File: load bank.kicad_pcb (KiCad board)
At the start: 2 copper layers, 95.4 x 80.6 mm, 28 parts, among them J1 25SH-B-02-TS, J10 25SH-B-02-TS, J11 EURO_BLOCK,_3_POSITION, J12 EURO_BLOCK,_3_POSITION, J2 LHD-03-TS, J3 EBBA-03-C-SS-BU, J4 25SH-B-02-TS, J5 Conn_01x02_Male, J6 Conn_01x02_Male, J7 696101000002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

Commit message: updated pcb with fan2 connector
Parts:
- added J13: 25SH-B-02-TS, Connector_JST:JST_EH_B2B-EH-A_1x02_P2.50mm_Vertical, F.Cu at (142.2, 87.9)
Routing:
- net +5V: track 30.8 -> 42.7 mm
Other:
- board text removed: "120V 7A"

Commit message: updated pcb layout with zener and resistor
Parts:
- added D5: 1N5230B, 1N5231B_R0:DIOAD928W47L399D179, F.Cu at (164.6, 92.2)
- added R6: 500R, Resistor_THT:R_Axial_DIN0207_L6.3mm_D2.5mm_P7.62mm_Horizontal, F.Cu at (161.3, 88.4)
- moved J5 7.52 mm to (162.1, 83.3)
- moved J11 2.76 mm to (158.3, 68.1)
- moved R5 0.25 mm to (167.9, 96.5)
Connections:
- D2 pad 2: +5V -> Net-(D2-A)
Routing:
- net Net-(D2-A): track 0.00 -> 7.56 mm
- net Net-(J5-Pin_1): track 8.75 -> 14.5 mm
- net Net-(D3-A): track 76.8 -> 79.2 mm
- net GNDA: track 108.8 -> 110.1 mm
- net /res_1: track 20.5 -> 19.5 mm
- net +5V: track 42.7 -> 41.9 mm

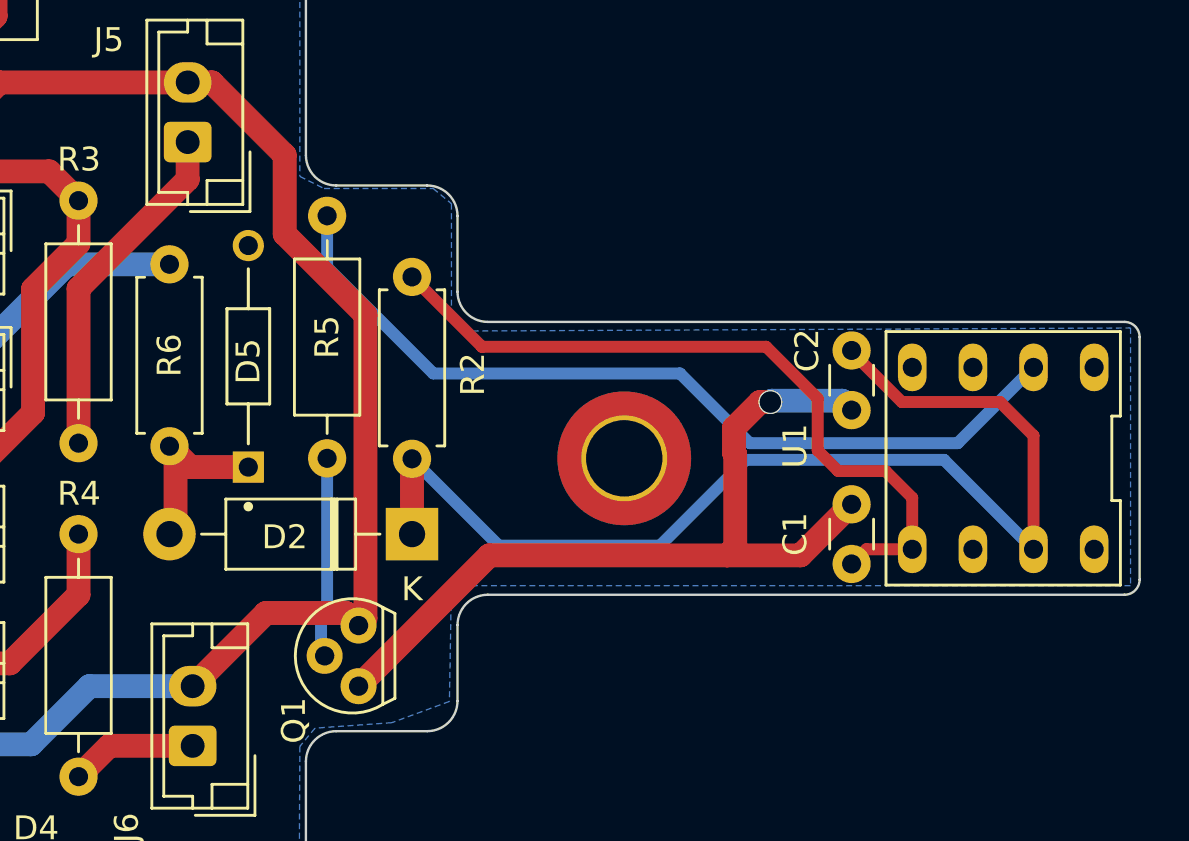
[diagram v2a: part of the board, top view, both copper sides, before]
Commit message: repositioned mounting hole
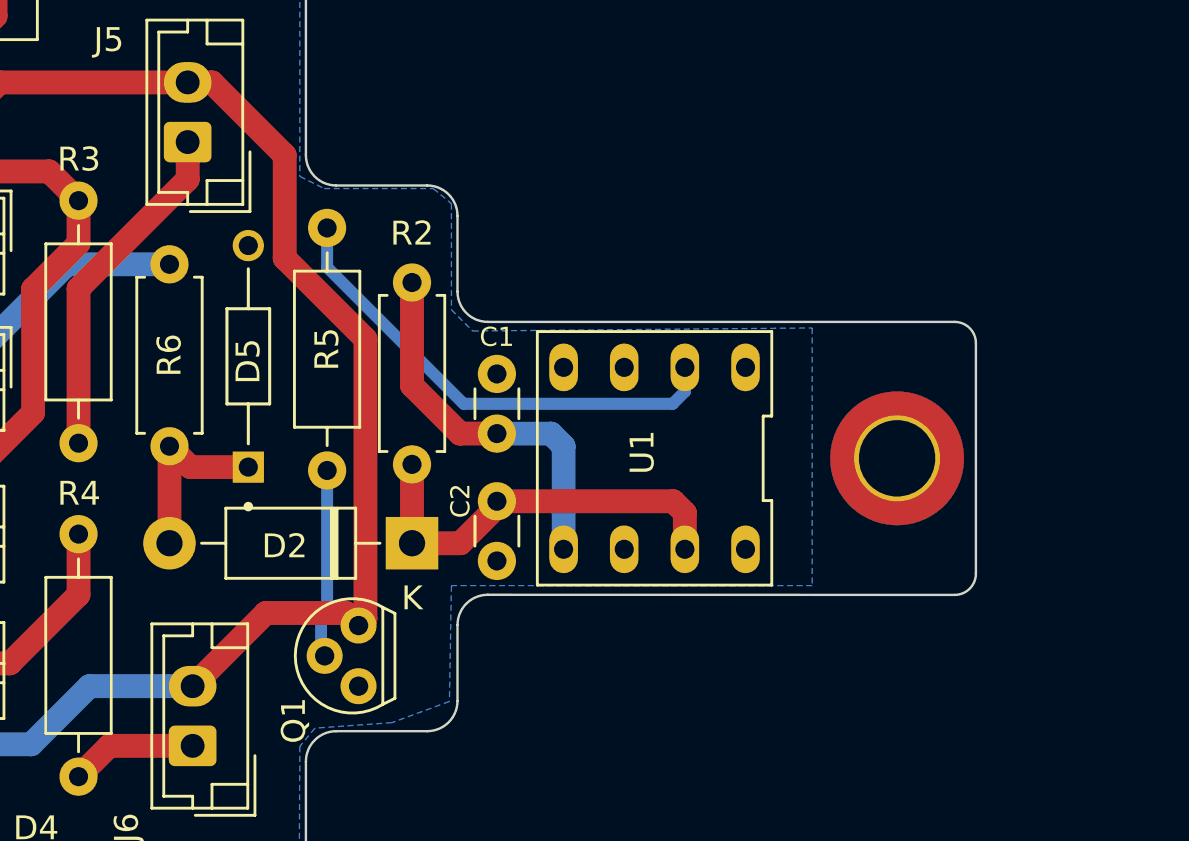
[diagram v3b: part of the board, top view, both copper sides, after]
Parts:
- moved C2 16.1 mm to (175.0, 98.3)
- moved C1 15.8 mm to (175.0, 93.0)
- moved U1 14.6 mm to (181.6, 96.5)
- moved H3 11.4 mm to (191.8, 96.5)
- moved R5 0.51 mm to (167.9, 97.0)
- moved D2 0.38 mm to (171.4, 100.1)
- moved R2 0.23 mm to (171.4, 96.8)
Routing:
- net GND: track 34.9 -> 0.00 mm, vias 1 -> 0
- net Net-(D2-K): track 47.6 -> 17.3 mm
- net T_CONTROL: track 36.1 -> 20.2 mm
- net Net-(U1-TSET): track 31.0 -> 16.3 mm
- net Net-(Q1-B): track 8.44 -> 7.93 mm
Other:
- board size 95.4 x 80.6 mm -> 88.5 x 80.6 mm
